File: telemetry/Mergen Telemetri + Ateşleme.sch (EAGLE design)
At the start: 81 parts, among them J2 U.FL, Q2 IRLML6344TRPBF, Q3 IRLML6344TRPBF, U1 STM32F401CCU6UFQFPN-48_7X7X0P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, U2 ADXL345BCCZ, U3 LPS22HB, U4 L86, U6 AMS1117-3.3, U7 AMS1117-3.3, Y1 ABM3B-26.000MHZ-10-1-U-T

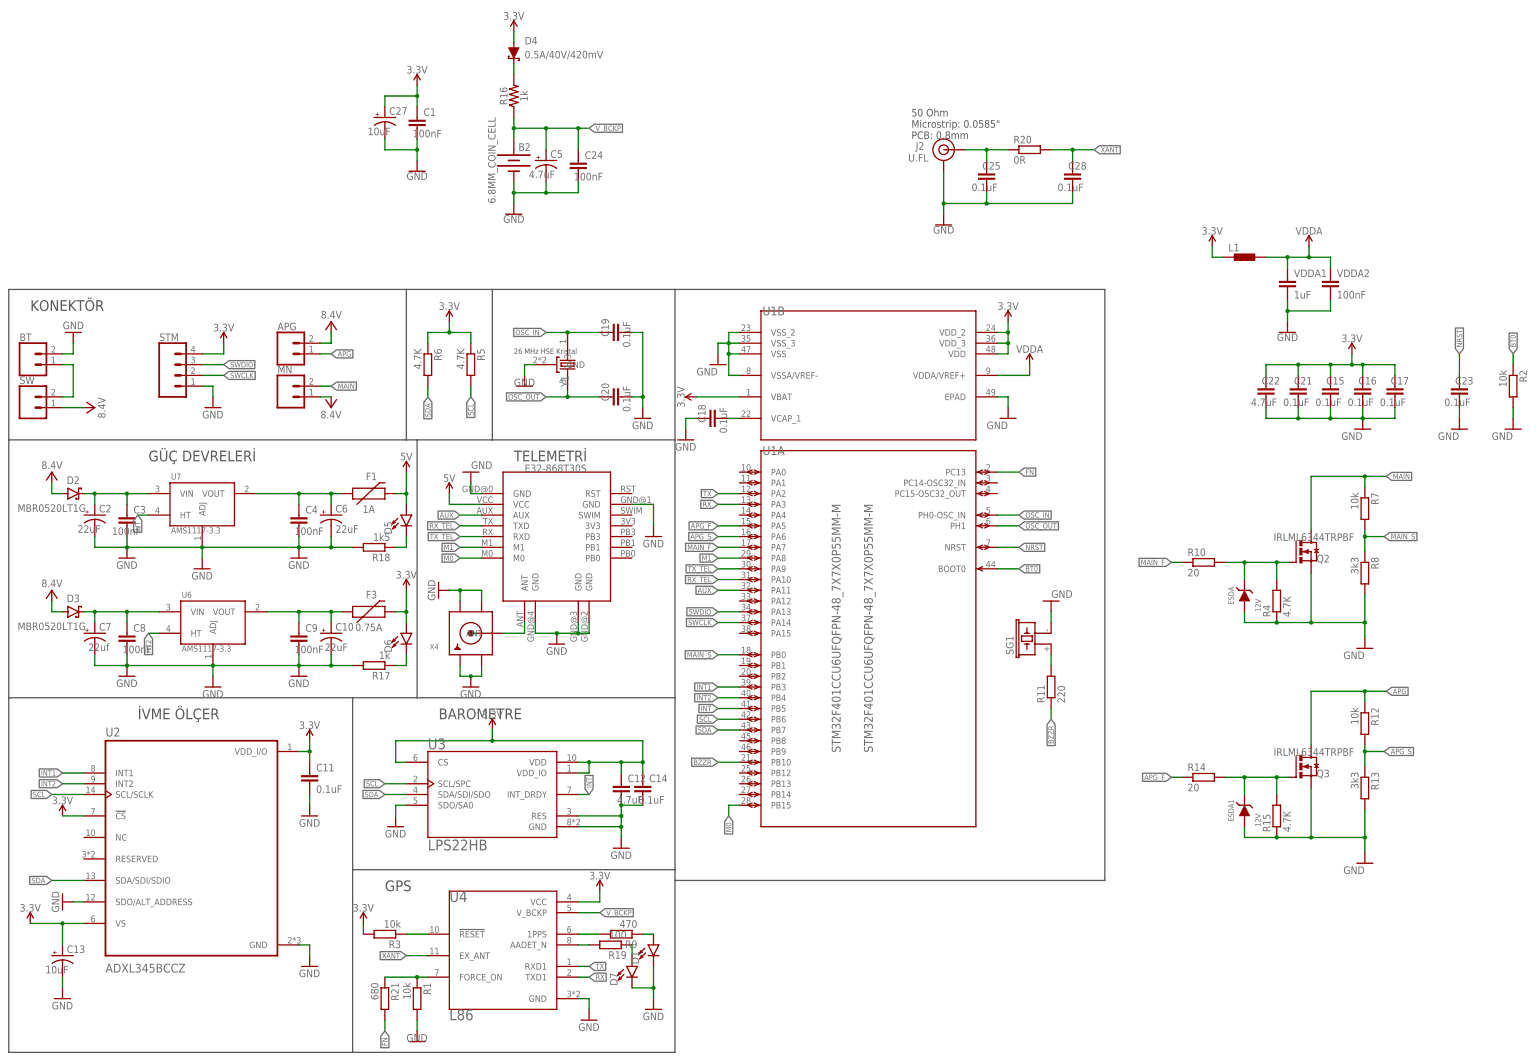
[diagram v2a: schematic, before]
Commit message: Extra polygon was added for methal distance and 1x4 JST connector was added for payload
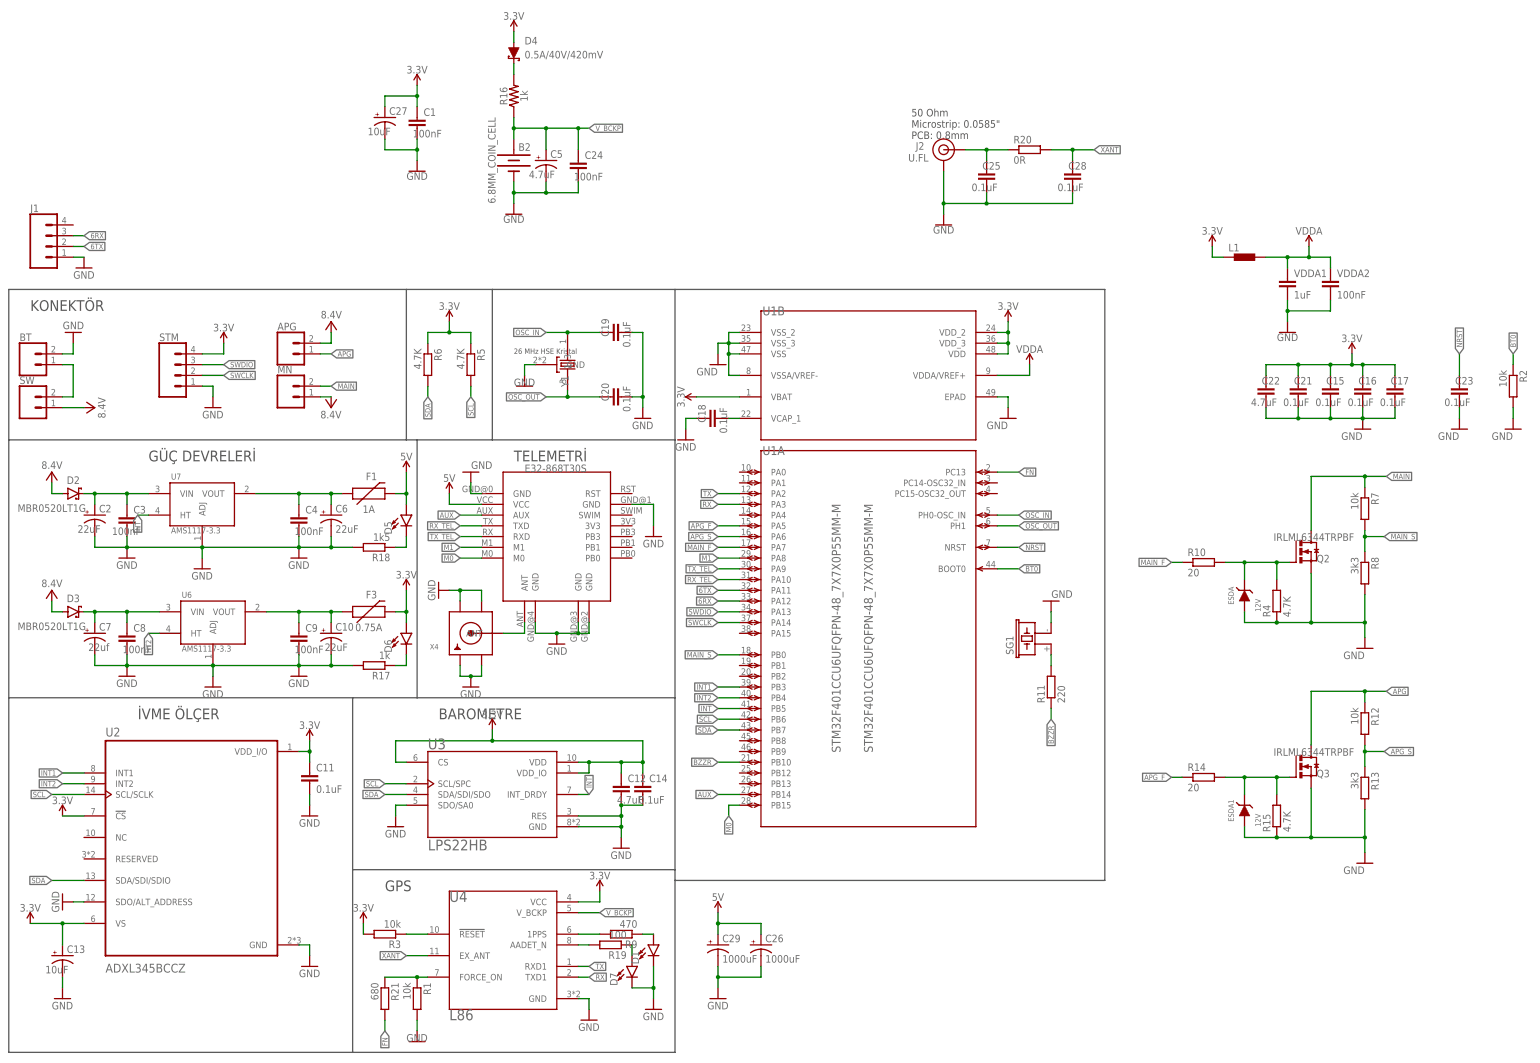
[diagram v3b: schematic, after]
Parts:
- added C26, C29: 1000uF, adafruit:CPOL-US150CLZ-1010
- added J1: (no value), SparkFun-Connectors:CONN_04JST-PTH-VERT
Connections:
- new net 6RX: J1.3, U1A.PA12
- new net 6TX: J1.2, U1A.PA11
- net 5V: now also C26.+, C29.+
- net AUX: now also U1A.PB14; no longer U1A.PA11
- net GND: now also C26.-, C29.-, J1.1
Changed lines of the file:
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@@
 <part name="ESDA1" library="Wurth_EMC Components_WE-TVSP" library_urn="urn:adsk.eagle:library:14283044" deviceset="WE-TVSP_DO-214AC_400W_UNI" device="" package3d_urn="urn:adsk.eagle:package:12146528/2" technology="_824500102" value="12V"/>
 <part name="R21" library="rcl" library_urn="urn:adsk.eagle:library:334" deviceset="R-EU_" device="R0402" package3d_urn="urn:adsk.eagle:package:23547/3" value="680"/>
+<part name="GND10" library="supply1" library_urn="urn:adsk.eagle:library:371" deviceset="GND" device=""/>
+<part name="SUPPLY17" library="SparkFun-PowerSymbols" library_urn="urn:adsk.eagle:library:530" deviceset="5V" device=""/>
+<part name="C29" library="adafruit" library_urn="urn:adsk.eagle:library:420" deviceset="CPOL-US" device="150CLZ-1010" package3d_urn="urn:adsk.eagle:package:6240454/1" value="1000uF"/>
+<part name="C26" library="adafruit" library_urn="urn:adsk.eagle:library:420" deviceset="CPOL-US" device="150CLZ-1010" package3d_urn="urn:adsk.eagle:package:6240454/1" value="1000uF"/>
+<part name="GND38" library="supply1" library_urn="urn:adsk.eagle:library:371" deviceset="GND" device=""/>
+<part name="J1" library="SparkFun-Connectors" library_urn="urn:adsk.eagle:library:513" deviceset="CONN_04" device="JST-PTH-VERT" package3d_urn="urn:adsk.eagle:package:38102/1"/>
 </parts>
 <sheets>
@@
 <attribute name="VALUE" x="-82.042" y="-77.47" size="1.778" layer="96" rot="R270"/>
 </instance>
+<instance part="GND10" gate="1" x="-149.86" y="91.44" smashed="yes">
+<attribute name="VALUE" x="-152.4" y="88.9" size="1.778" layer="96"/>
+</instance>
+<instance part="SUPPLY17" gate="G$1" x="0" y="-60.96" smashed="yes">
+<attribute name="VALUE" x="0" y="-58.166" size="1.778" layer="96" align="bottom-center"/>
+</instance>
+<instance part="C29" gate="G$1" x="0" y="-68.58" smashed="yes">
+<attribute name="NAME" x="1.016" y="-67.945" size="1.778" layer="95"/>
+<attribute name="VALUE" x="1.016" y="-72.771" size="1.778" layer="96"/>
+</instance>
+<instance part="C26" gate="G$1" x="10.16" y="-68.58" smashed="yes">
+<attribute name="NAME" x="11.176" y="-67.945" size="1.778" layer="95"/>
+<attribute name="VALUE" x="11.176" y="-72.771" size="1.778" layer="96"/>
+</instance>
+<instance part="GND38" gate="1" x="0" y="-81.28" smashed="yes">
+<attribute name="VALUE" x="-2.54" y="-83.82" size="1.778" layer="96"/>
+</instance>
+<instance part="J1" gate="G$1" x="-157.48" y="96.52" smashed="yes">
+<attribute name="VALUE" x="-162.56" y="89.154" size="1.778" layer="96" font="vector"/>
+<attribute name="NAME" x="-162.56" y="104.648" size="1.778" layer="95" font="vector"/>
+</instance>
 </instances>
 <busses>
@@
 <junction x="63.5" y="106.68"/>
 </segment>
+<segment>
+<pinref part="GND10" gate="1" pin="GND"/>
+<pinref part="J1" gate="G$1" pin="1"/>
+<wire x1="-152.4" y1="93.98" x2="-149.86" y2="93.98" width="0.1524" layer="91"/>
+</segment>
+<segment>
+<pinref part="C29" gate="G$1" pin="-"/>
+<pinref part="GND38" gate="1" pin="GND"/>
+<wire x1="0" y1="-73.66" x2="0" y2="-76.2" width="0.1524" layer="91"/>
+<pinref part="C26" gate="G$1" pin="-"/>
+<wire x1="0" y1="-76.2" x2="0" y2="-78.74" width="0.1524" layer="91"/>
+<wire x1="10.16" y1="-73.66" x2="10.16" y2="-76.2" width="0.1524" layer="91"/>
+<wire x1="10.16" y1="-76.2" x2="0" y2="-76.2" width="0.1524" layer="91"/>
+<junction x="0" y="-76.2"/>
+</segment>
 </net>
 <net name="N$4" class="0">
@@
 <net name="AUX" class="0">
 <segment>
-<pinref part="U1" gate="A" pin="PA11"/>
-<wire x1="5.08" y1="15.24" x2="0" y2="15.24" width="0.1524" layer="91"/>
-<label x="0" y="15.24" size="1.27" layer="95" rot="R180" xref="yes"/>
-</segment>
-<segment>
 <pinref part="U5" gate="G$1" pin="AUX"/>
 <wire x1="-55.88" y1="33.02" x2="-60.96" y2="33.02" width="0.1524" layer="91"/>
 <label x="-60.96" y="33.02" size="1.27" layer="95" rot="R180" xref="yes"/>
+</segment>
+<segment>
+<pinref part="U1" gate="A" pin="PB14"/>
+<wire x1="5.08" y1="-33.02" x2="0" y2="-33.02" width="0.1524" layer="91"/>
+<label x="0" y="-33.02" size="1.27" layer="95" rot="R180" xref="yes"/>
 </segment>
 </net>
@@
 <pinref part="U5" gate="G$1" pin="VCC"/>
 <wire x1="-63.5" y1="35.56" x2="-55.88" y2="35.56" width="0.1524" layer="91"/>
+</segment>
+<segment>
+<pinref part="SUPPLY17" gate="G$1" pin="5V"/>
+<pinref part="C29" gate="G$1" pin="+"/>
+<wire x1="0" y1="-60.96" x2="0" y2="-63.5" width="0.1524" layer="91"/>
+<pinref part="C26" gate="G$1" pin="+"/>
+<wire x1="0" y1="-63.5" x2="0" y2="-66.04" width="0.1524" layer="91"/>
+<wire x1="10.16" y1="-66.04" x2="10.16" y2="-63.5" width="0.1524" layer="91"/>
+<wire x1="10.16" y1="-63.5" x2="0" y2="-63.5" width="0.1524" layer="91"/>
+<junction x="0" y="-63.5"/>
 </segment>
 </net>
@@
 </segment>
 </net>
+<net name="6TX" class="0">
+<segment>
+<pinref part="U1" gate="A" pin="PA11"/>
+<wire x1="5.08" y1="15.24" x2="0" y2="15.24" width="0.1524" layer="91"/>
+<label x="0" y="15.24" size="1.27" layer="95" rot="R180" xref="yes"/>
+</segment>
+<segment>
+<label x="-149.86" y="96.52" size="1.27" layer="95" xref="yes"/>
+<pinref part="J1" gate="G$1" pin="2"/>
+<wire x1="-152.4" y1="96.52" x2="-149.86" y2="96.52" width="0.1524" layer="91"/>
+</segment>
+</net>
+<net name="6RX" class="0">
+<segment>
+<pinref part="U1" gate="A" pin="PA12"/>
+<wire x1="5.08" y1="12.7" x2="0" y2="12.7" width="0.1524" layer="91"/>
+<label x="0" y="12.7" size="1.27" layer="95" rot="R180" xref="yes"/>
+</segment>
+<segment>
+<label x="-149.86" y="99.06" size="1.27" layer="95" xref="yes"/>
+<pinref part="J1" gate="G$1" pin="3"/>
+<wire x1="-152.4" y1="99.06" x2="-149.86" y2="99.06" width="0.1524" layer="91"/>
+</segment>
+</net>
